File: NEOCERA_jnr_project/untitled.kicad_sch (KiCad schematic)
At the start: 4 parts, among them U4 HCPL-2630, U5 HCPL-2630, U6 HCPL-2630, U7 HCPL-2630

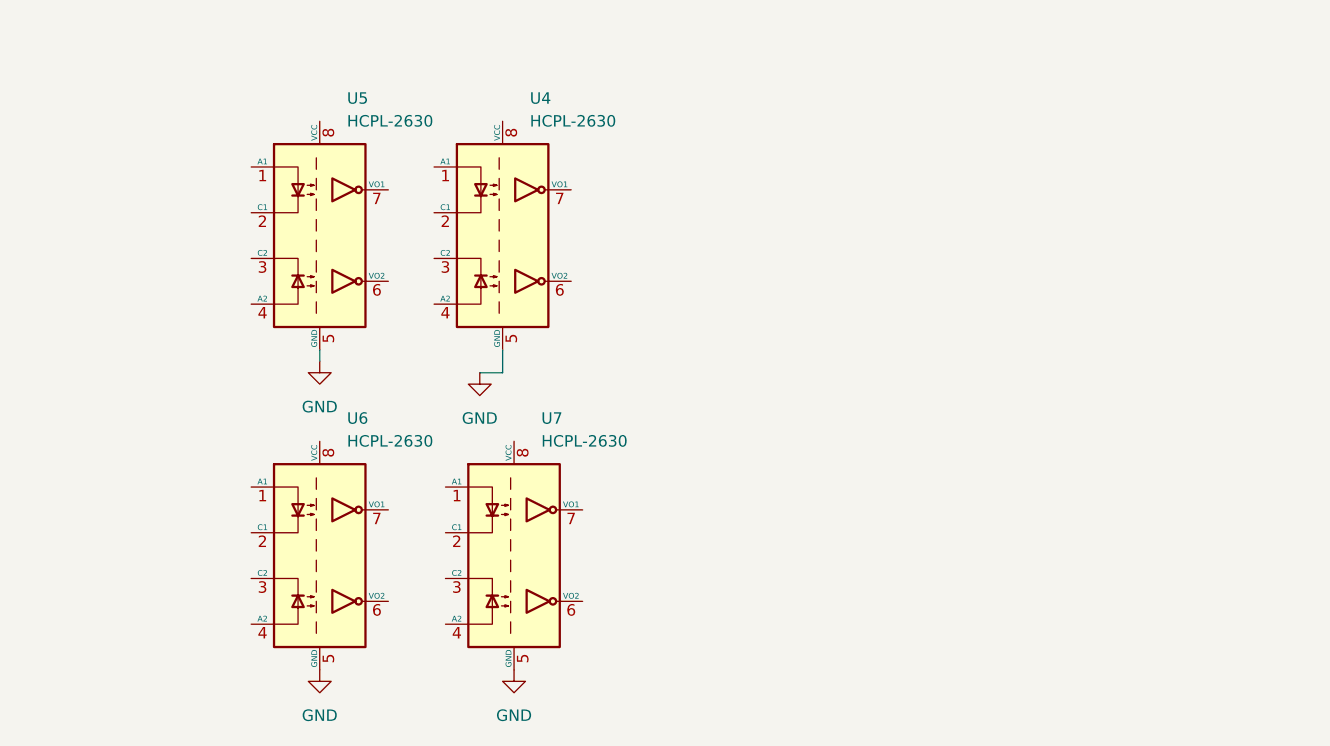
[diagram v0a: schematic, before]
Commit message: Edits made with Dr. Caw.
I added the net to the root
I added the write global nets to some of the previously designed symbols like TX/RX
I added a 3.3V pullup resistor to the opto
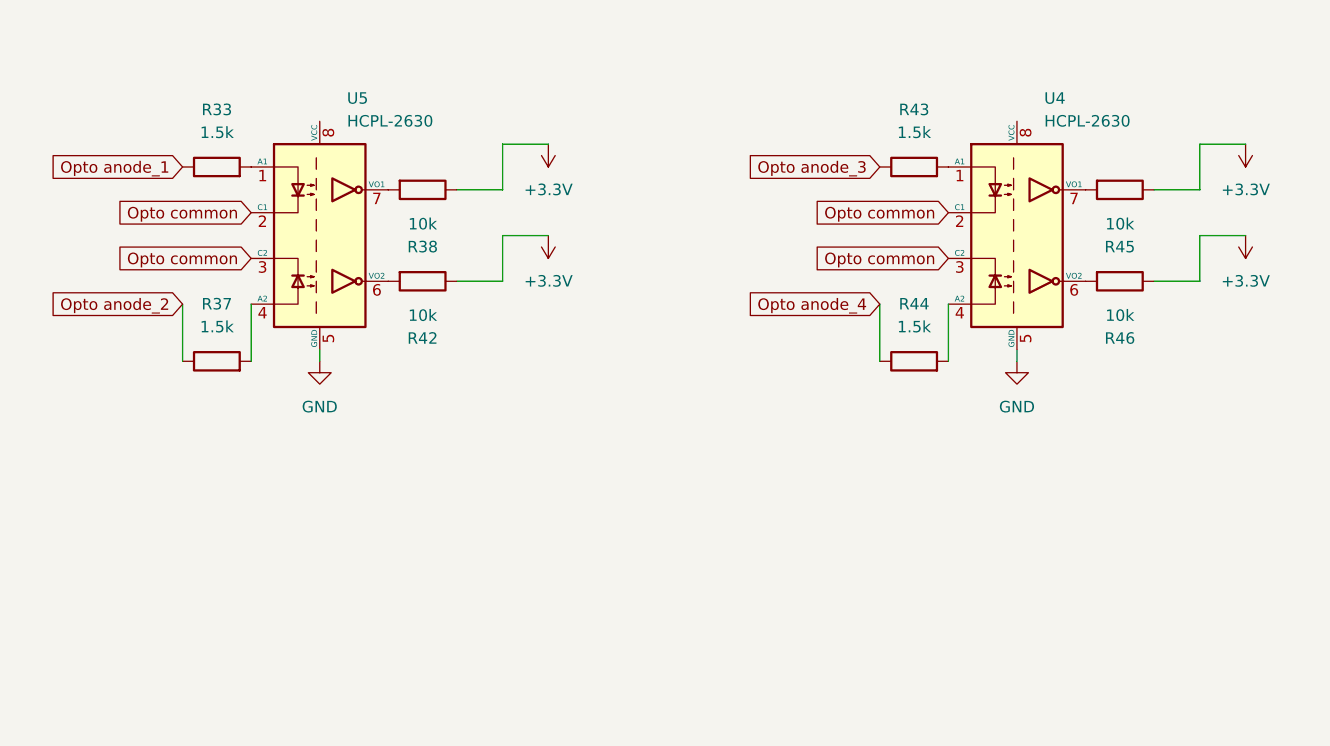
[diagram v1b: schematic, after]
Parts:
- removed U6, U7: HCPL-2630, Package_DIP:DIP-8_W7.62mm, symbol Isolator:HCPL-2630
- added R33, R37, R43, R44: 1.5k, Resistor_SMD:R_0805_2012Metric_Pad1.20x1.40mm_HandSolder, symbol Device:R
- added R38, R42, R45, R46: 10k, Resistor_SMD:R_0603_1608Metric_Pad0.98x0.95mm_HandSolder, symbol Device:R
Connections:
- net at U5.1 (A1): now also R33.2
- net Opto common: now reaches U5.2 (C1)
- net Opto common: now also U4.2 (C1), U4.3 (C2), U5.3 (C2)
- net at U5.4 (A2): now also R37.2
- net at U5.6 (VO2): now also R42.2
- net at U5.7 (VO1): now also R38.2
- net at U4.1 (A1): now also R43.2
- net at U4.4 (A2): now also R44.2
- net at U4.6 (VO2): now also R46.2
- net at U4.7 (VO1): now also R45.2
- new net +3.3V: R38.1, R42.1, R45.1, R46.1
- new net Opto anode_1: R33.1
- new net Opto anode_2: R37.1
- new net Opto anode_3: R43.1
- new net Opto anode_4: R44.1

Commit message: bunch of edits
bunch of edits were done including DB37
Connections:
- net opto_output4: now reaches R46.2, U4.6 (VO2)
- net opto_output3: now reaches R45.2, U4.7 (VO1)
- net +5V: now reaches U4.8 (VCC)
- net +5V: now also U5.8 (VCC)
- net opto_output1: now reaches R38.2, U5.7 (VO1)
- net opto_output2: now reaches R42.2, U5.6 (VO2)
- removed net Opto common: U4.2 (C1), U4.3 (C2), U5.2 (C1), U5.3 (C2)
- new net Opto common1: U5.2 (C1)
- new net Opto common2: U5.3 (C2)
- new net Opto common3: U4.2 (C1)
- new net Opto common4: U4.3 (C2)
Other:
- moved on the sheet: R38, R45
